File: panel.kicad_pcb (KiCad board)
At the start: 2 copper layers, 145.4 x 94 mm, 112 parts, among them J1 Conn_01x05, J2 Conn_01x05, J3 Screw_Terminal

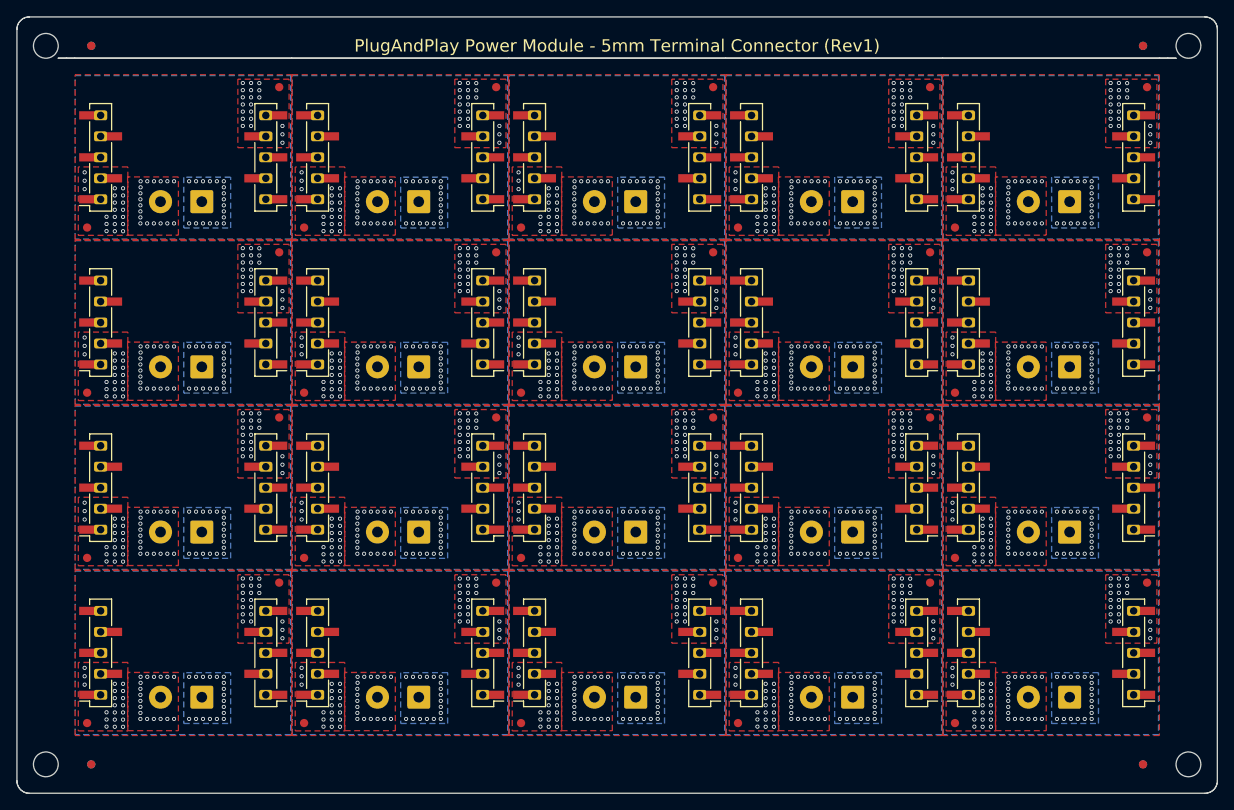
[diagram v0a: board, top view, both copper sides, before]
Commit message: Increase header connectors paste openning by 5%. Decrease screw terminal holes from 2.3mm to 2.2mm.
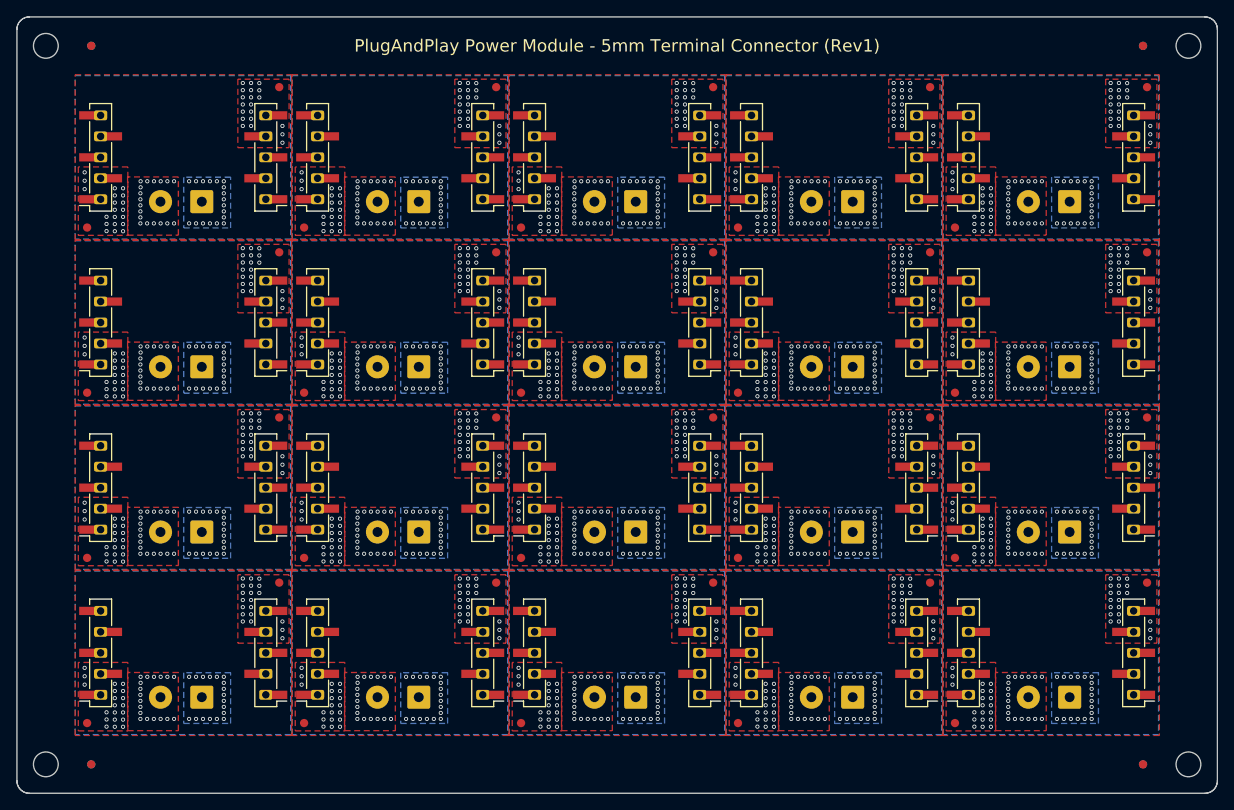
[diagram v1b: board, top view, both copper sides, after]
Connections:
- net Board_0-unconnected-(J1-Pin_3-Pad3)_1 renamed Board_0-unconnected-(J1-Pin_3-Pad3)
- net Board_0-unconnected-(J2-Pin_3-Pad3)_1 renamed Board_0-unconnected-(J2-Pin_3-Pad3)
- net Board_1-unconnected-(J1-Pin_3-Pad3)_1 renamed Board_1-unconnected-(J1-Pin_3-Pad3)
- net Board_1-unconnected-(J2-Pin_3-Pad3)_1 renamed Board_1-unconnected-(J2-Pin_3-Pad3)
- net Board_10-unconnected-(J1-Pin_3-Pad3)_1 renamed Board_10-unconnected-(J1-Pin_3-Pad3)
- net Board_10-unconnected-(J2-Pin_3-Pad3)_1 renamed Board_10-unconnected-(J2-Pin_3-Pad3)
- net Board_11-unconnected-(J1-Pin_3-Pad3)_1 renamed Board_11-unconnected-(J1-Pin_3-Pad3)
- net Board_11-unconnected-(J2-Pin_3-Pad3)_1 renamed Board_11-unconnected-(J2-Pin_3-Pad3)
- net Board_12-unconnected-(J1-Pin_3-Pad3)_1 renamed Board_12-unconnected-(J1-Pin_3-Pad3)
- net Board_12-unconnected-(J2-Pin_3-Pad3)_1 renamed Board_12-unconnected-(J2-Pin_3-Pad3)
- net Board_13-unconnected-(J1-Pin_3-Pad3)_1 renamed Board_13-unconnected-(J1-Pin_3-Pad3)
- net Board_13-unconnected-(J2-Pin_3-Pad3)_1 renamed Board_13-unconnected-(J2-Pin_3-Pad3)
- net Board_14-unconnected-(J1-Pin_3-Pad3)_1 renamed Board_14-unconnected-(J1-Pin_3-Pad3)
- net Board_14-unconnected-(J2-Pin_3-Pad3)_1 renamed Board_14-unconnected-(J2-Pin_3-Pad3)
- net Board_15-unconnected-(J1-Pin_3-Pad3)_1 renamed Board_15-unconnected-(J1-Pin_3-Pad3)
- net Board_15-unconnected-(J2-Pin_3-Pad3)_1 renamed Board_15-unconnected-(J2-Pin_3-Pad3)
- net Board_16-unconnected-(J1-Pin_3-Pad3)_1 renamed Board_16-unconnected-(J1-Pin_3-Pad3)
- net Board_16-unconnected-(J2-Pin_3-Pad3)_1 renamed Board_16-unconnected-(J2-Pin_3-Pad3)
- net Board_17-unconnected-(J1-Pin_3-Pad3)_1 renamed Board_17-unconnected-(J1-Pin_3-Pad3)
- net Board_17-unconnected-(J2-Pin_3-Pad3)_1 renamed Board_17-unconnected-(J2-Pin_3-Pad3)
- net Board_18-unconnected-(J1-Pin_3-Pad3)_1 renamed Board_18-unconnected-(J1-Pin_3-Pad3)
- net Board_18-unconnected-(J2-Pin_3-Pad3)_1 renamed Board_18-unconnected-(J2-Pin_3-Pad3)
- net Board_19-unconnected-(J1-Pin_3-Pad3)_1 renamed Board_19-unconnected-(J1-Pin_3-Pad3)
- net Board_19-unconnected-(J2-Pin_3-Pad3)_1 renamed Board_19-unconnected-(J2-Pin_3-Pad3)
- net Board_2-unconnected-(J1-Pin_3-Pad3)_1 renamed Board_2-unconnected-(J1-Pin_3-Pad3)
- net Board_2-unconnected-(J2-Pin_3-Pad3)_1 renamed Board_2-unconnected-(J2-Pin_3-Pad3)
- net Board_3-unconnected-(J1-Pin_3-Pad3)_1 renamed Board_3-unconnected-(J1-Pin_3-Pad3)
- net Board_3-unconnected-(J2-Pin_3-Pad3)_1 renamed Board_3-unconnected-(J2-Pin_3-Pad3)
- net Board_4-unconnected-(J1-Pin_3-Pad3)_1 renamed Board_4-unconnected-(J1-Pin_3-Pad3)
- net Board_4-unconnected-(J2-Pin_3-Pad3)_1 renamed Board_4-unconnected-(J2-Pin_3-Pad3)
- net Board_5-unconnected-(J1-Pin_3-Pad3)_1 renamed Board_5-unconnected-(J1-Pin_3-Pad3)
- net Board_5-unconnected-(J2-Pin_3-Pad3)_1 renamed Board_5-unconnected-(J2-Pin_3-Pad3)
- net Board_6-unconnected-(J1-Pin_3-Pad3)_1 renamed Board_6-unconnected-(J1-Pin_3-Pad3)
- net Board_6-unconnected-(J2-Pin_3-Pad3)_1 renamed Board_6-unconnected-(J2-Pin_3-Pad3)
- net Board_7-unconnected-(J1-Pin_3-Pad3)_1 renamed Board_7-unconnected-(J1-Pin_3-Pad3)
- net Board_7-unconnected-(J2-Pin_3-Pad3)_1 renamed Board_7-unconnected-(J2-Pin_3-Pad3)
- net Board_8-unconnected-(J1-Pin_3-Pad3)_1 renamed Board_8-unconnected-(J1-Pin_3-Pad3)
- net Board_8-unconnected-(J2-Pin_3-Pad3)_1 renamed Board_8-unconnected-(J2-Pin_3-Pad3)
- net Board_9-unconnected-(J1-Pin_3-Pad3)_1 renamed Board_9-unconnected-(J1-Pin_3-Pad3)
- net Board_9-unconnected-(J2-Pin_3-Pad3)_1 renamed Board_9-unconnected-(J2-Pin_3-Pad3)
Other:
- outline, holes or cut-outs redrawn
